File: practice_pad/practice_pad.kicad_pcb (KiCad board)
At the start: 2 copper layers, 105.2 x 148.1 mm, 43 parts, among them SW1 SW_Push_45deg, SW10 SW_Push_45deg, SW11 SW_Push_45deg, SW12 SW_Push_45deg, SW13 SW_Push_45deg, SW14 SW_Push_45deg, SW15 SW_Push_45deg, SW16 SW_Push_45deg, SW17 SW_Push_45deg, SW18 SW_Push_45deg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

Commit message: a little more routing
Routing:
- net Net-(SW12-Pad1): track 0.00 -> 121.3 mm
- net Net-(SW1-Pad1): track 0.00 -> 118.2 mm
- net Net-(SW11-Pad1): track 0.00 -> 118.2 mm
- net Net-(SW10-Pad1): track 0.00 -> 94.4 mm
- net Net-(D1-K): track 20.5 -> 40.9 mm
- net Net-(D4-A): track 0.00 -> 11.4 mm
- net Net-(D2-A): track 0.00 -> 11.4 mm
- net Net-(D3-A): track 0.00 -> 11.4 mm

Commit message: only a few traces left
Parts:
- added 2uStab: Stabilizer_Cherry_MX_2.00u, PCM_Mounting_Keyboard_Stabilizer:Stabilizer_Cherry_MX_2.00u, F.Cu at (57.1, 152.4)
- added 2uStab: Stabilizer_Cherry_MX_2.00u, PCM_Mounting_Keyboard_Stabilizer:Stabilizer_Cherry_MX_2.00u, F.Cu at (114.3, 147.6)
- added 2uStab: Stabilizer_Cherry_MX_2.00u, PCM_Mounting_Keyboard_Stabilizer:Stabilizer_Cherry_MX_2.00u, F.Cu at (114.3, 109.5)
- moved D12 38.1 mm to (109.5, 111.9)
- moved D19 38.1 mm to (109.5, 150.0)
- moved SW12 38.1 mm to (114.3, 109.5)
- moved SW19 38.1 mm to (114.3, 147.6)
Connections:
- D19 pad 1: Net-(D16-K) -> Net-(D13-K)
- SW10 pad 1: Net-(SW10-Pad1) -> Net-(U1-GP8)
- SW14 pad 1: Net-(SW10-Pad1) -> Net-(U1-GP8)
- SW17 pad 1: Net-(SW10-Pad1) -> Net-(U1-GP8)
- SW2 pad 1: Net-(SW10-Pad1) -> Net-(U1-GP8)
- SW6 pad 1: Net-(SW10-Pad1) -> Net-(U1-GP8)
- U1 pad 9: unconnected-(U1-GP8-Pad9) -> Net-(U1-GP8)
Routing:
- net Net-(U1-GP8): track 0.00 -> 112.7 mm
- net Net-(SW10-Pad1): track 94.4 -> 0.00 mm
- net Net-(D13-K): track 0.00 -> 78.4 mm
- net Net-(D5-K): track 0.00 -> 68.8 mm
- net Net-(D1-K): track 40.9 -> 104.9 mm
- net Net-(D10-K): track 0.00 -> 60.6 mm
- net Net-(D16-K): track 0.00 -> 42.8 mm
- net Net-(D20-K): track 0.00 -> 38.8 mm
- net Net-(D19-A): track 0.00 -> 11.4 mm
- net Net-(D8-A): track 0.00 -> 11.4 mm
- net Net-(D12-A): track 0.00 -> 11.4 mm
- net Net-(D20-A): track 0.00 -> 11.4 mm
- net Net-(D13-A): track 0.00 -> 11.4 mm
- net Net-(D9-A): track 0.00 -> 11.4 mm
- net Net-(D5-A): track 0.00 -> 11.4 mm
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
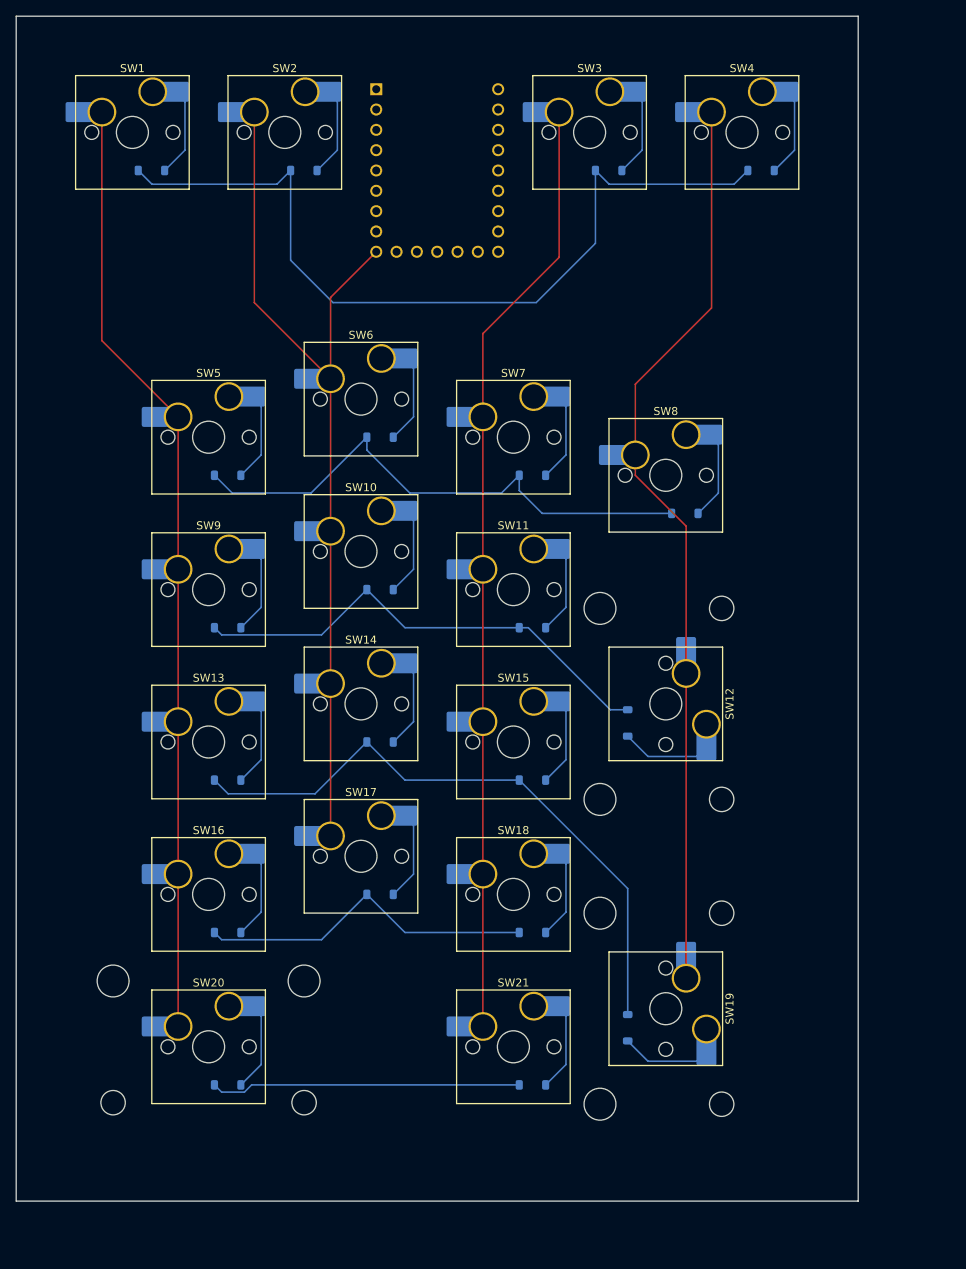
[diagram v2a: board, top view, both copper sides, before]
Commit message: updated switch footprints
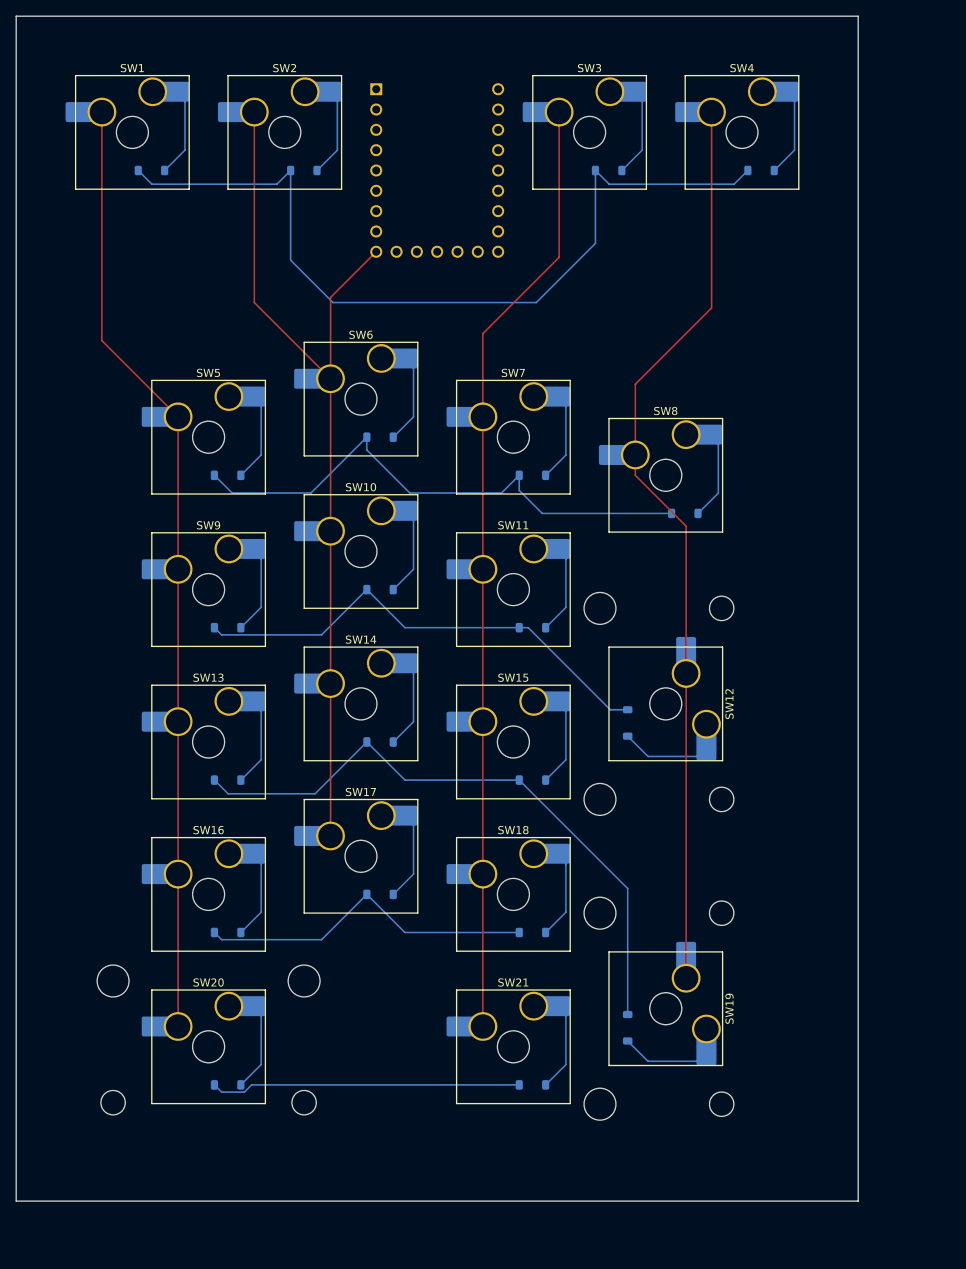
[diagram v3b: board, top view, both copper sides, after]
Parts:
- SW1, SW10, SW11, SW13, SW14, SW15, SW16, SW17, SW18, SW2, SW21, SW3, SW4, SW5, SW6, SW7, SW8, SW9: footprint PCM_Switch_Keyboard_Hotswap_Kailh:SW_Hotswap_Kailh_MX_Plated_1.00u -> maxwellmods:SW_Hotswap_Kailh_MX_Plated_PlateMount_1.00u
- SW12, SW19, SW20: footprint PCM_Switch_Keyboard_Hotswap_Kailh:SW_Hotswap_Kailh_MX_Plated_2.00u -> maxwellmods:SW_Hotswap_Kailh_MX_Plated_PlateMount_2.00u

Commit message: just about done
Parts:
- moved D11 13.1 mm to (109.0, 106.5)
- moved D12 13.1 mm to (120.9, 118.4)
- moved D15 13.1 mm to (109.0, 125.5)
- moved D21 13.1 mm to (109.0, 163.6)
- moved D4 13.1 mm to (137.6, 49.3)
- moved U1 13.1 mm to (97.1, 49.3)
- moved SW4 13.1 mm to (135.2, 44.6)
- moved D7 13.1 mm to (109.0, 87.4)
- moved 2uStab 13.1 mm to (68.6, 158.9)
- moved SW13 13.1 mm to (68.6, 120.8)
- moved SW16 13.1 mm to (68.6, 139.8)
- moved SW20 13.1 mm to (68.6, 158.9)
- moved SW5 13.1 mm to (68.6, 82.7)
- moved SW9 13.1 mm to (68.6, 101.7)
- moved 2uStab 13.1 mm to (125.7, 154.1)
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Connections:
- SW1 pad 1: Net-(SW1-Pad1) -> Net-(U1-GP1)
- SW11 pad 1: Net-(SW11-Pad1) -> Net-(U1-GP28)
- SW12 pad 1: Net-(SW12-Pad1) -> Net-(U1-GP29)
- SW13 pad 1: Net-(SW1-Pad1) -> Net-(U1-GP1)
- SW15 pad 1: Net-(SW11-Pad1) -> Net-(U1-GP28)
- SW16 pad 1: Net-(SW1-Pad1) -> Net-(U1-GP1)
- SW18 pad 1: Net-(SW11-Pad1) -> Net-(U1-GP28)
- SW19 pad 1: Net-(SW12-Pad1) -> Net-(U1-GP29)
- SW20 pad 1: Net-(SW1-Pad1) -> Net-(U1-GP1)
- SW21 pad 1: Net-(SW11-Pad1) -> Net-(U1-GP28)
- SW3 pad 1: Net-(SW11-Pad1) -> Net-(U1-GP28)
- SW4 pad 1: Net-(SW12-Pad1) -> Net-(U1-GP29)
- SW5 pad 1: Net-(SW1-Pad1) -> Net-(U1-GP1)
- SW7 pad 1: Net-(SW11-Pad1) -> Net-(U1-GP28)
- SW8 pad 1: Net-(SW12-Pad1) -> Net-(U1-GP29)
- SW9 pad 1: Net-(SW1-Pad1) -> Net-(U1-GP1)
- U1 pad 10: unconnected-(U1-GP9-Pad10) -> Net-(D5-K)
- U1 pad 11: unconnected-(U1-GP10-Pad11) -> Net-(D10-K)
- U1 pad 12: unconnected-(U1-GP11-Pad12) -> Net-(D13-K)
- U1 pad 13: unconnected-(U1-GP12-Pad13) -> Net-(D16-K)
- U1 pad 14: unconnected-(U1-GP13-Pad14) -> Net-(D20-K)
- U1 pad 18: unconnected-(U1-GP27-Pad18) -> Net-(D1-K)
- U1 pad 19: unconnected-(U1-GP28-Pad19) -> Net-(U1-GP28)
- U1 pad 2: unconnected-(U1-GP1-Pad2) -> Net-(U1-GP1)
- U1 pad 20: unconnected-(U1-GP29-Pad20) -> Net-(U1-GP29)
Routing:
- net Net-(U1-GP1): track 0.00 -> 159.4 mm
- net Net-(U1-GP29): track 0.00 -> 155.5 mm
- net Net-(U1-GP28): track 0.00 -> 127.6 mm
- net Net-(SW1-Pad1): track 119.7 -> 0.00 mm
- net Net-(SW11-Pad1): track 118.2 -> 0.00 mm
- net Net-(SW12-Pad1): track 117.7 -> 0.00 mm
- net Net-(D20-K): track 38.8 -> 155.8 mm, vias 0 -> 3
- net Net-(D16-K): track 42.8 -> 128.0 mm, vias 0 -> 1
- net Net-(D13-K): track 78.4 -> 143.3 mm, vias 0 -> 1
- net Net-(D10-K): track 60.6 -> 113.2 mm, vias 0 -> 1
- net Net-(D5-K): track 68.8 -> 107.3 mm, vias 0 -> 1
- net Net-(D1-K): track 104.9 -> 118.2 mm
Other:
- board text added: "100% leak-free comfort"
- board text added: "maxipad v1"

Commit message: Ready to Build
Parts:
- SW1, SW10, SW11, SW12, SW13, SW14, SW15, SW16, SW17, SW18, SW19, SW2, SW20, SW21, SW3, SW4, SW5, SW6, SW7, SW8, SW9: value SW_Push_45deg -> SW_HS
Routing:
- net Net-(D20-K): track 155.8 -> 161.6 mm
- net Net-(D10-K): track 113.2 -> 114.4 mm
- net Net-(D16-K): track 128.0 -> 129.1 mm

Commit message: update layout for pcb
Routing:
- net Net-(D20-A): track 11.4 -> 9.64 mm
- net Net-(D7-A): track 11.4 -> 10.5 mm
- net Net-(D21-A): track 11.4 -> 10.5 mm
- net Net-(D17-A): track 11.4 -> 10.5 mm
- net Net-(D2-A): track 11.4 -> 10.5 mm
- net Net-(D1-A): track 11.4 -> 10.5 mm
- net Net-(D6-A): track 11.4 -> 10.5 mm
- net Net-(D18-A): track 11.4 -> 10.5 mm
- net Net-(D15-A): track 11.4 -> 10.5 mm
- net Net-(D14-A): track 11.4 -> 10.5 mm
- net Net-(D12-A): track 11.4 -> 10.5 mm
- net Net-(D11-A): track 11.4 -> 10.5 mm
- net Net-(D10-A): track 11.4 -> 10.5 mm
- net Net-(D8-A): track 11.4 -> 10.5 mm
- net Net-(D5-A): track 11.4 -> 10.5 mm
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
